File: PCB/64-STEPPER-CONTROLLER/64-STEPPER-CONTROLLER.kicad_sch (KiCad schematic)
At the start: 3 parts

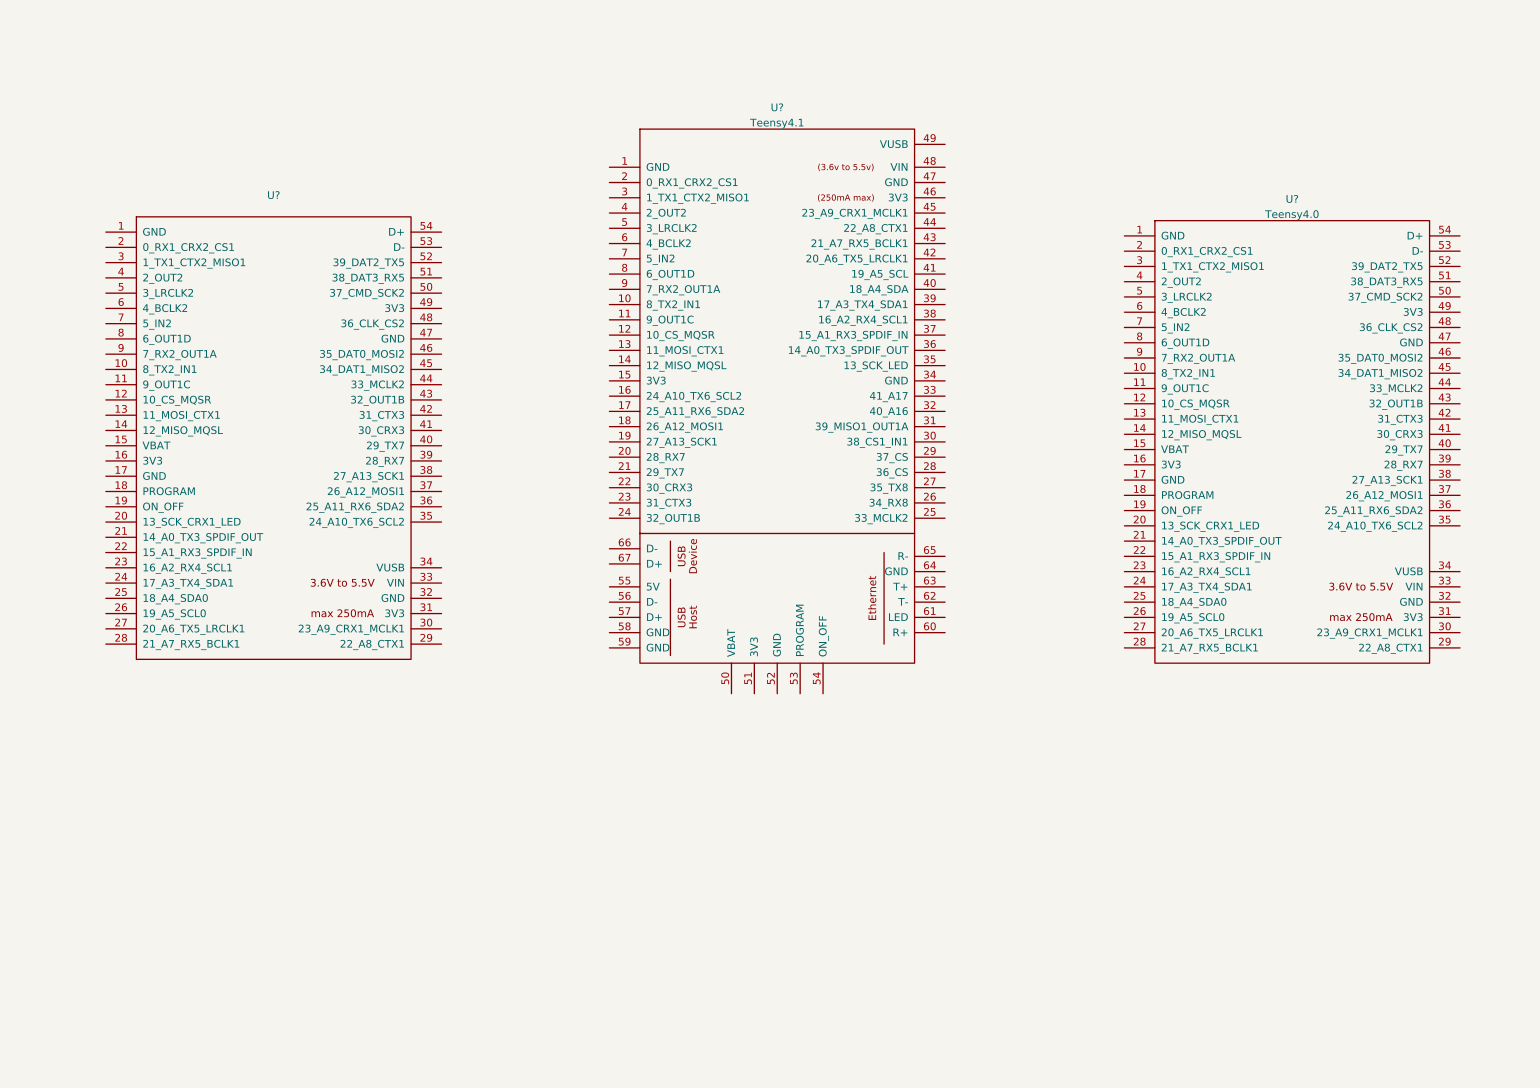
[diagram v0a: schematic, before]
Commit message: 64 motor initial setup
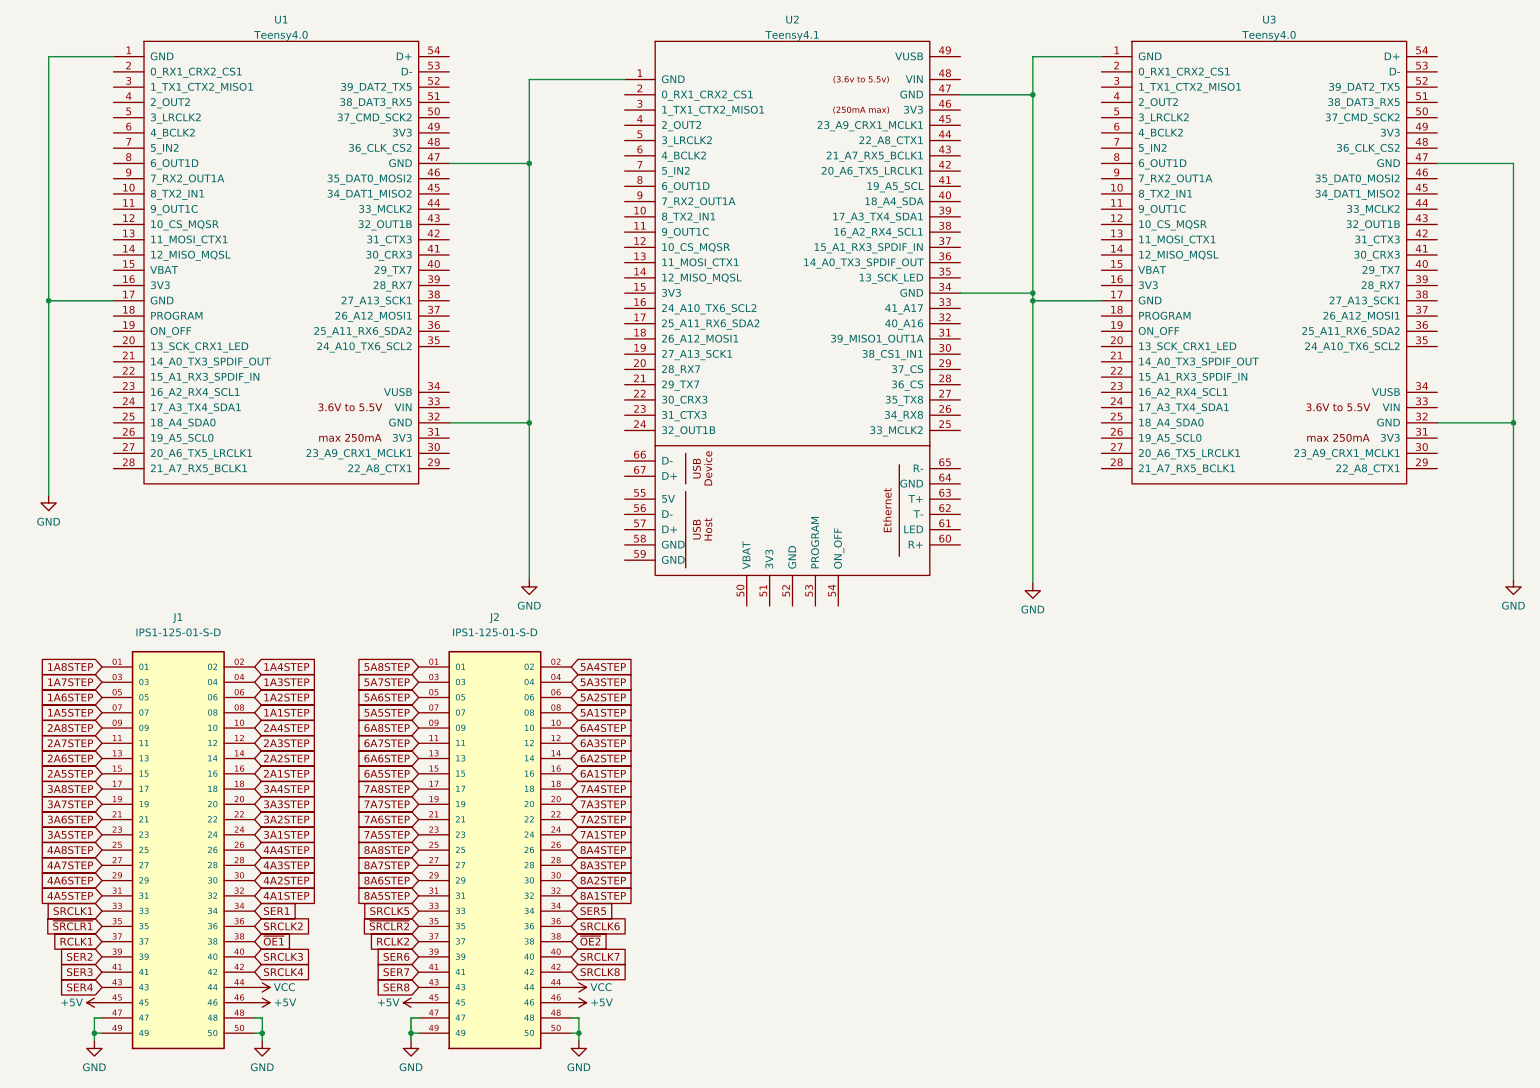
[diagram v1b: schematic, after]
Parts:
- added J1, J2: IPS1-125-01-S-D, SAMTEC_IPS1-125-01-S-D, symbol IPS1-125-01-S-D:IPS1-125-01-S-D
- U1: renamed from U?; value (none) -> Teensy4.0; footprint (none) -> LIBRARIES:Teensy40
- U2: renamed from U?; footprint (none) -> LIBRARIES:Teensy41
- U3: renamed from U?; footprint (none) -> LIBRARIES:Teensy40
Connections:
- net GND: now reaches U1.1 (GND)
- net GND: now also U1.17 (GND), U1.32 (GND), U1.47 (GND), U2.1 (GND), U2.34 (GND), U2.47 (GND), U3.1 (GND), U3.17 (GND), U3.32 (GND), U3.47 (GND), J1.47, J1.48, J1.49, J1.50, J2.47, J2.48, J2.49, J2.50
- new net +5V: J1.45, J1.46, J2.45, J2.46
- new net 1A1STEP: J1.08
- new net 1A2STEP: J1.06
- new net 1A3STEP: J1.04
- new net 1A4STEP: J1.02
- new net 1A5STEP: J1.07
- new net 1A6STEP: J1.05
- new net 1A7STEP: J1.03
- new net 1A8STEP: J1.01
- new net 2A1STEP: J1.16
- new net 2A2STEP: J1.14
- new net 2A3STEP: J1.12
- new net 2A4STEP: J1.10
- new net 2A5STEP: J1.15
- new net 2A6STEP: J1.13
- new net 2A7STEP: J1.11
- new net 2A8STEP: J1.09
- new net 3A1STEP: J1.24
- new net 3A2STEP: J1.22
- new net 3A3STEP: J1.20
- new net 3A4STEP: J1.18
- new net 3A5STEP: J1.23
- new net 3A6STEP: J1.21
- new net 3A7STEP: J1.19
- new net 3A8STEP: J1.17
- new net 4A1STEP: J1.32
- new net 4A2STEP: J1.30
- new net 4A3STEP: J1.28
- new net 4A4STEP: J1.26
- new net 4A5STEP: J1.31
- new net 4A6STEP: J1.29
- new net 4A7STEP: J1.27
- new net 4A8STEP: J1.25
- new net 5A1STEP: J2.08
- new net 5A2STEP: J2.06
- new net 5A3STEP: J2.04
- new net 5A4STEP: J2.02
- new net 5A5STEP: J2.07
- new net 5A6STEP: J2.05
- new net 5A7STEP: J2.03
- new net 5A8STEP: J2.01
- new net 6A1STEP: J2.16
- new net 6A2STEP: J2.14
- new net 6A3STEP: J2.12
- new net 6A4STEP: J2.10
- new net 6A5STEP: J2.15
- new net 6A6STEP: J2.13
- new net 6A7STEP: J2.11
- new net 6A8STEP: J2.09
- new net 7A1STEP: J2.24
- new net 7A2STEP: J2.22
- new net 7A3STEP: J2.20
- new net 7A4STEP: J2.18
- new net 7A5STEP: J2.23
- new net 7A6STEP: J2.21
- new net 7A7STEP: J2.19
- new net 7A8STEP: J2.17
- new net 8A1STEP: J2.32
- new net 8A2STEP: J2.30
- new net 8A3STEP: J2.28
- new net 8A4STEP: J2.26
- new net 8A5STEP: J2.31
- new net 8A6STEP: J2.29
- new net 8A7STEP: J2.27
- new net 8A8STEP: J2.25
- new net RCLK1: J1.37
- new net RCLK2: J2.37
- new net SER1: J1.34
- new net SER2: J1.39
- new net SER3: J1.41
- new net SER4: J1.43
- new net SER5: J2.34
- new net SER6: J2.39
- new net SER7: J2.41
- new net SER8: J2.43
- new net SRCLK1: J1.33
- new net SRCLK2: J1.36
- new net SRCLK3: J1.40
- new net SRCLK4: J1.42
- new net SRCLK5: J2.33
- new net SRCLK6: J2.36
- new net SRCLK7: J2.40
- new net SRCLK8: J2.42
- new net VCC: J1.44, J2.44
- new net ~{OE1}: J1.38
- new net ~{OE2}: J2.38
- new net ~{SRCLR1}: J1.35
- new net ~{SRCLR2}: J2.35
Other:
- moved on the sheet: U1, U2, U3

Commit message: progress
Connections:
- net +5V: now also U1.33 (VIN), U2.48 (VIN), U3.33 (VIN)
- net 1A1STEP: now also U1.2 (0_RX1_CRX2_CS1)
- net 1A2STEP: now also U1.3 (1_TX1_CTX2_MISO1)
- net 1A3STEP: now also U1.4 (2_OUT2)
- net 1A4STEP: now also U1.5 (3_LRCLK2)
- net 1A5STEP: now also U1.6 (4_BCLK2)
- net 1A6STEP: now also U1.9 (7_RX2_OUT1A)
- net 1A7STEP: now also U1.10 (8_TX2_IN1)
- net 1A8STEP: now also U1.11 (9_OUT1C)
- net 2A1STEP: now also U1.12 (10_CS_MQSR)
- net 2A2STEP: now also U1.13 (11_MOSI_CTX1)
- net 2A3STEP: now also U1.14 (12_MISO_MQSL)
- net 2A4STEP: now also U1.20 (13_SCK_CRX1_LED)
- net 2A5STEP: now also U1.21 (14_A0_TX3_SPDIF_OUT)
- net 2A6STEP: now also U1.22 (15_A1_RX3_SPDIF_IN)
- net 2A7STEP: now also U1.23 (16_A2_RX4_SCL1)
- net 2A8STEP: now also U1.24 (17_A3_TX4_SDA1)
- net 3A1STEP: now also U1.25 (18_A4_SDA0)
- net 3A2STEP: now also U1.26 (19_A5_SCL0)
- net 3A3STEP: now also U1.27 (20_A6_TX5_LRCLK1)
- net 3A4STEP: now also U1.28 (21_A7_RX5_BCLK1)
- net 3A5STEP: now also U1.29 (22_A8_CTX1)
- net 3A6STEP: now also U1.30 (23_A9_CRX1_MCLK1)
- net 3A7STEP: now also U1.35 (24_A10_TX6_SCL2)
- net 3A8STEP: now also U1.36 (25_A11_RX6_SDA2)
- net 4A1STEP: now also U1.37 (26_A12_MOSI1)
- net 4A2STEP: now also U1.38 (27_A13_SCK1)
- net 4A3STEP: now also U1.39 (28_RX7)
- net 4A4STEP: now also U1.40 (29_TX7)
- net 4A5STEP: now also U1.41 (30_CRX3)
- net 4A6STEP: now also U1.42 (31_CTX3)
- net 4A7STEP: now also U1.43 (32_OUT1B)
- net 4A8STEP: now also U1.44 (33_MCLK2)
- net 5A1STEP: now also U3.2 (0_RX1_CRX2_CS1)
- net 5A2STEP: now also U3.3 (1_TX1_CTX2_MISO1)
- net 5A3STEP: now also U3.4 (2_OUT2)
- net 5A4STEP: now also U3.5 (3_LRCLK2)
- net 5A5STEP: now also U3.6 (4_BCLK2)
- net 5A6STEP: now also U3.7 (5_IN2)
- net 5A7STEP: now also U3.8 (6_OUT1D)
- net 5A8STEP: now also U3.9 (7_RX2_OUT1A)
- net 6A1STEP: now also U3.10 (8_TX2_IN1)
- net 6A2STEP: now also U3.11 (9_OUT1C)
- net 6A3STEP: now also U3.12 (10_CS_MQSR)
- net 6A4STEP: now also U3.13 (11_MOSI_CTX1)
- net 6A5STEP: now also U3.14 (12_MISO_MQSL)
- net 6A6STEP: now also U3.21 (14_A0_TX3_SPDIF_OUT)
- net 6A7STEP: now also U3.22 (15_A1_RX3_SPDIF_IN)
- net 6A8STEP: now also U3.23 (16_A2_RX4_SCL1)
- net 7A1STEP: now also U3.24 (17_A3_TX4_SDA1)
- net 7A2STEP: now also U3.25 (18_A4_SDA0)
- net 7A3STEP: now also U3.26 (19_A5_SCL0)
- net 7A4STEP: now also U3.27 (20_A6_TX5_LRCLK1)
- net 7A5STEP: now also U3.28 (21_A7_RX5_BCLK1)
- net 7A6STEP: now also U3.29 (22_A8_CTX1)
- net 7A7STEP: now also U3.30 (23_A9_CRX1_MCLK1)
- net 7A8STEP: now also U3.35 (24_A10_TX6_SCL2)
- net 8A1STEP: now also U3.36 (25_A11_RX6_SDA2)
- net 8A2STEP: now also U3.37 (26_A12_MOSI1)
- net 8A3STEP: now also U3.38 (27_A13_SCK1)
- net 8A4STEP: now also U3.39 (28_RX7)
- net 8A5STEP: now also U3.40 (29_TX7)
- net 8A6STEP: now also U3.41 (30_CRX3)
- net 8A7STEP: now also U3.42 (31_CTX3)
- net 8A8STEP: now also U3.43 (32_OUT1B)
- net GND: no longer U1.17 (GND), U1.47 (GND), U3.17 (GND), U3.47 (GND)
- no-connect marks 0 -> 55
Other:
- moved on the sheet: U3
